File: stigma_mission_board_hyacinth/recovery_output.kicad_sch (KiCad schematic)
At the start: 19 parts, among them Q6 DMN2056U, Q7 AOSP21321, Q8 DMN2056U, Q9 AOSP21321, U9 INA181

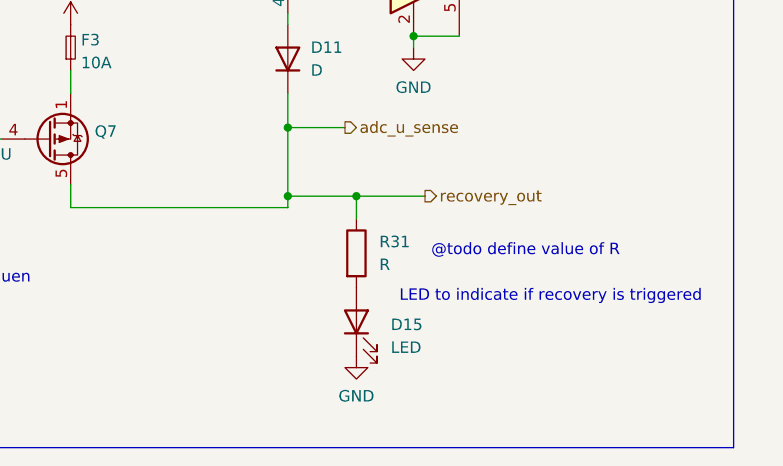
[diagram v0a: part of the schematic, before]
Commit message: rename recovery_output file
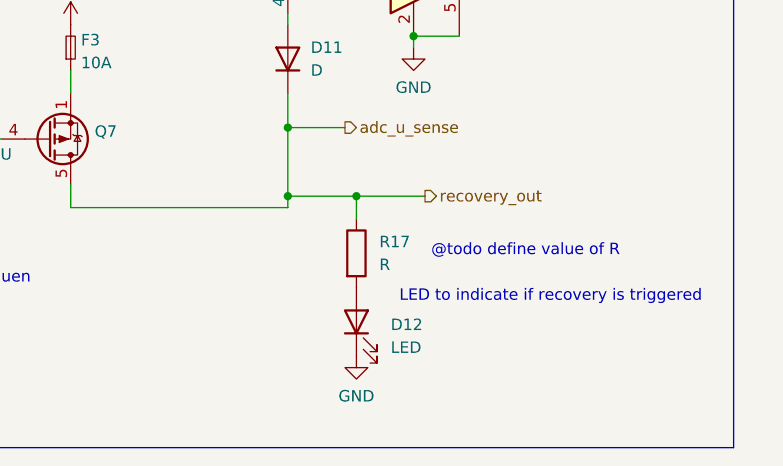
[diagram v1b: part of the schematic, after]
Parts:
- renumbered D15 to D12, R31 to R17

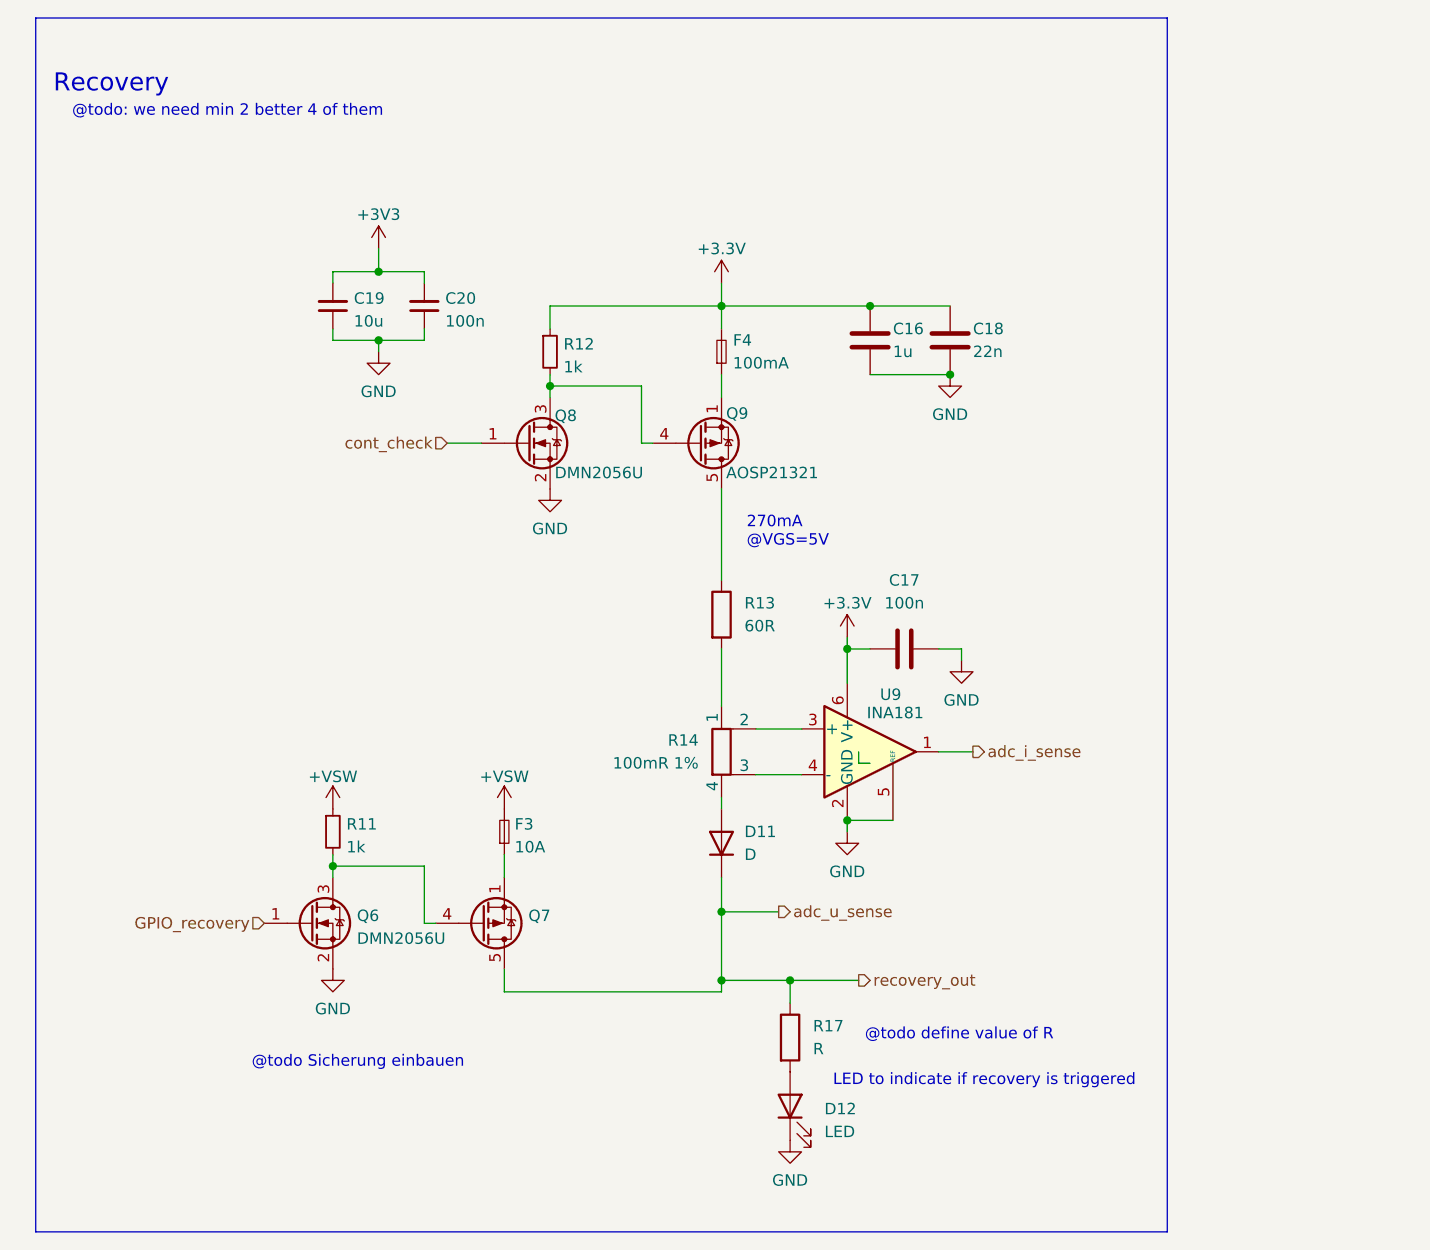
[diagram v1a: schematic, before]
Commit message: fix ethernet, add VH bus, fix voltage sensing
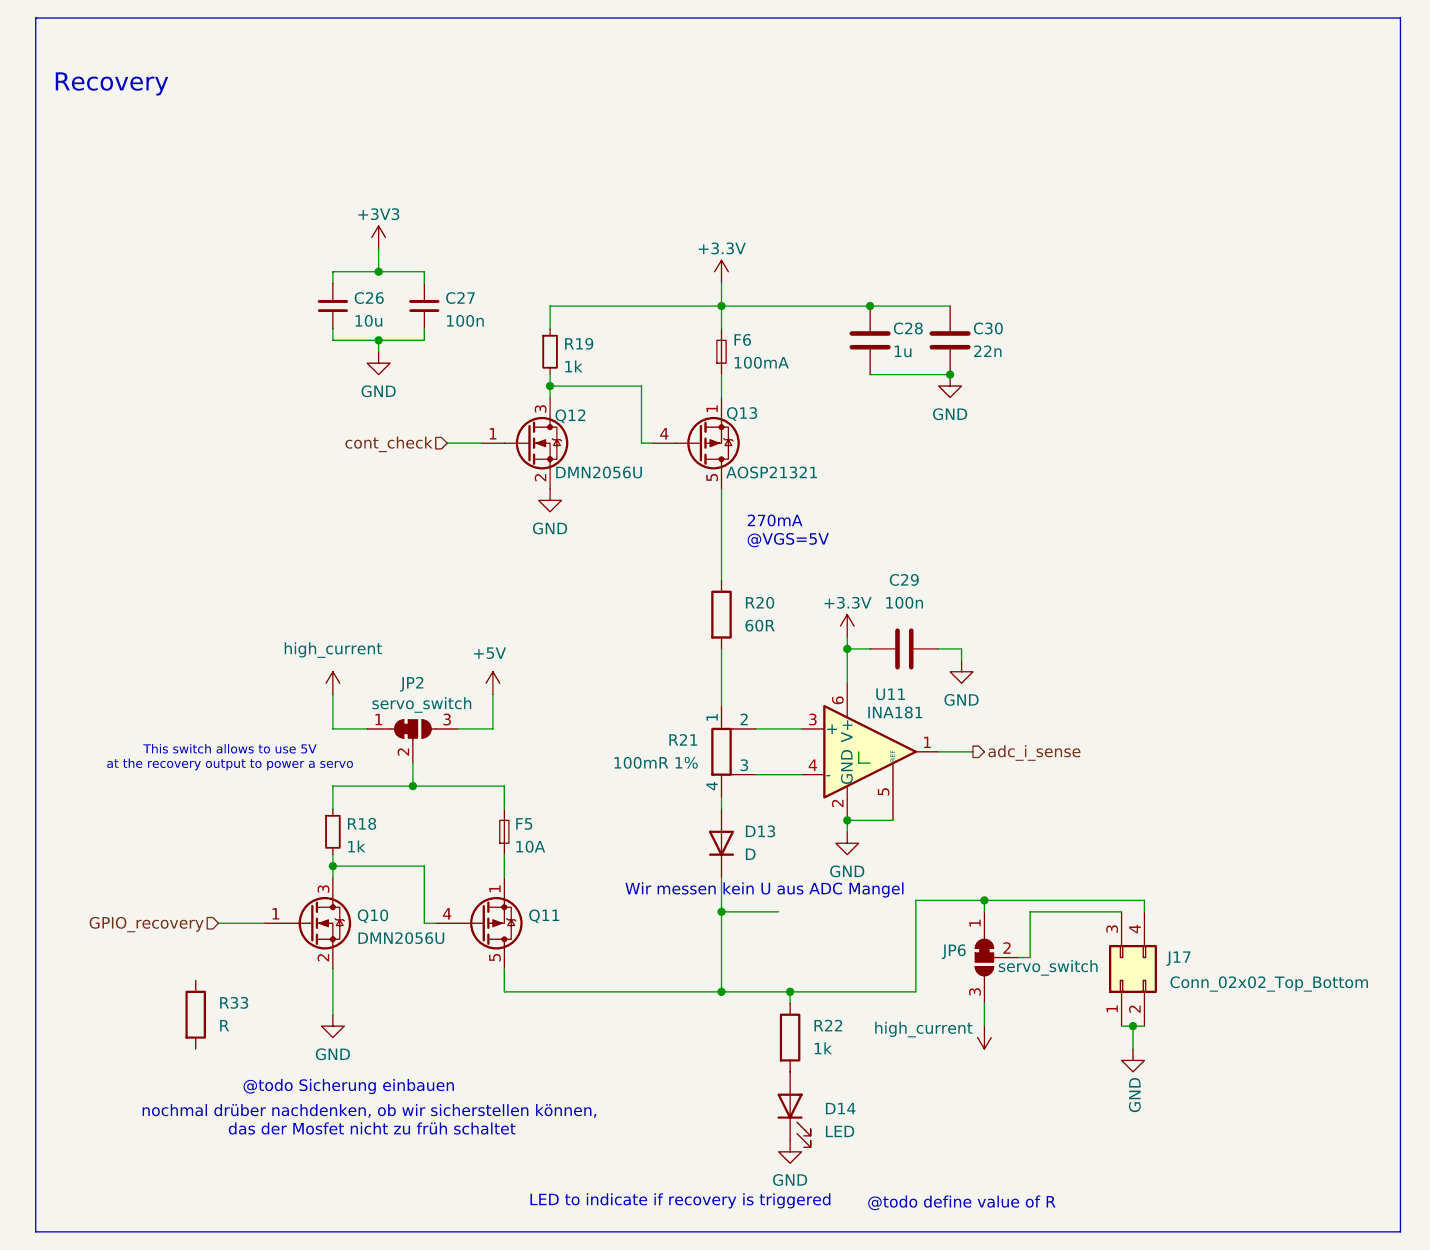
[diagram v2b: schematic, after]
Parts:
- added J17: Conn_02x02_Top_Bottom, symbol Connector_Generic:Conn_02x02_Top_Bottom
- added JP2, JP6: servo_switch, Jumper:SolderJumper-3_P1.3mm_Open_RoundedPad1.0x1.5mm, symbol Jumper:SolderJumper_3_Bridged12
- added R33: R, symbol Device:R
- R22: renamed from R17; value R -> 1k
- renumbered C19 to C26, C20 to C27, C16 to C28, C17 to C29, C18 to C30, D11 to D13, D12 to D14, F3 to F5, F4 to F6, Q6 to Q10, Q7 to Q11, Q8 to Q12, Q9 to Q13, R11 to R18, R12 to R19, R13 to R20, R14 to R21, U9 to U11
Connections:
- net GND: now also J17.1 (Pin_1), J17.2 (Pin_2)
- net +VSW: no longer names the net of F5.2, R18.1
- net +VSW: now also JP2.2 (C)
- net adc_u_sense: no longer names the net of D13.1 (K), Q11.5 (D), Q11.6 (D), Q11.7 (D), Q11.8 (D), R22.1
- net adc_u_sense: now also J17.4 (Pin_4), JP6.1 (A)
- new net: J17.3 (Pin_3), JP6.2 (C)
- new net +5V: JP2.3 (B)
- new net high_current: JP2.1 (A), JP6.3 (B)
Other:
- note added: "This switch allows to use 5V at the recovery output to power a servo"
- note added: "Wir messen kein U aus ADC Mangel"
- note added: "nochmal drüber nachdenken, ob wir sicherstellen können, das der Mosfet nicht zu früh schaltet"
- note removed: "@todo: we need min 2 better 4 of them"

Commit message: fixed a few small issues, added some part numbers and footprints
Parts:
- added C66: 10u, Capacitor_SMD:C_1206_3216Metric, symbol Device:C
- D13: value D -> NRVB130T1G; footprint (none) -> Diode_SMD:D_SOD-123; LCSC# (none) -> C917121
- R33: value R -> 10k
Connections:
- net GND: now also R33.2, C66.2
- net GPIO_recovery: now also R33.1
- net high_current: no longer JP6.3 (B)
- net adc_u_sense: now reaches D13.2 (A), R21.4
- net at F5.1, Q11.1 (S), Q11.2 (S)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: now also C66.1
- new net pwm_sig: JP6.3 (B)
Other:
- note added: "D"
- note added: "G"
- note added: "S"
- note added: "nochmal drüber nachdenken, ob wir sicherstellen können, das der Mosfet nicht zu früh schaltet -> ist kondensator ausreichend? -> verzögerung der spannung an DS"
- note removed: "@todo Sicherung einbauen"
- note removed: "Wir messen kein U aus ADC Mangel"
- note removed: "nochmal drüber nachdenken, ob wir sicherstellen können, das der Mosfet nicht zu früh schaltet"
- moved on the sheet: D13, J17, JP6, R33

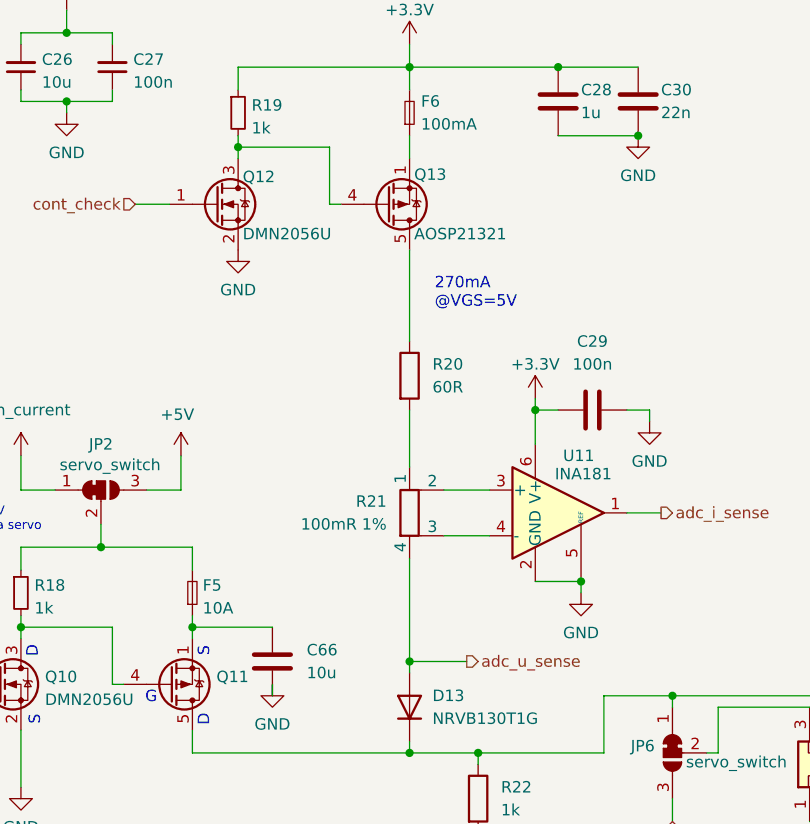
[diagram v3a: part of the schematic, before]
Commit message: changed mosfet to more suitable one
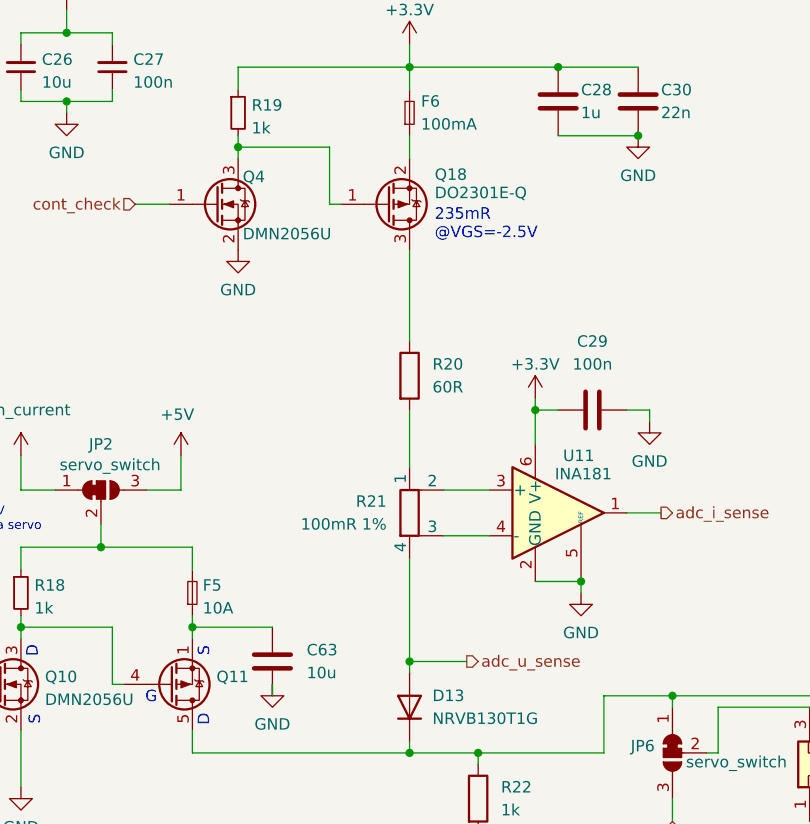
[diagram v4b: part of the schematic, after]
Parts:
- removed Q12: DMN2056U, Package_TO_SOT_SMD:SOT-23, symbol Transistor_FET:DMG2302U
- removed Q13: AOSP21321, Package_SO:SO-8_3.9x4.9mm_P1.27mm, symbol euroc_fc:AOSP21321
- added Q18: DO2301E-Q, Package_TO_SOT_SMD:SOT-23, symbol euroc_fc:AOSP21321
- added Q4: DMN2056U, Package_TO_SOT_SMD:SOT-23, symbol Transistor_FET:DMG2302U
- renumbered C66 to C63
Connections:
- net GND: now also Q4.2 (S)
- net cont_check: now also Q4.1 (G)
- net at R19.2: now also Q18.1 (G), Q4.3 (D)
- net at F6.1: now also Q18.2 (S)
- net at R20.1: now also Q18.3 (D)
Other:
- note added: "235mR @VGS=-2.5V"
- note removed: "270mA @VGS=5V"

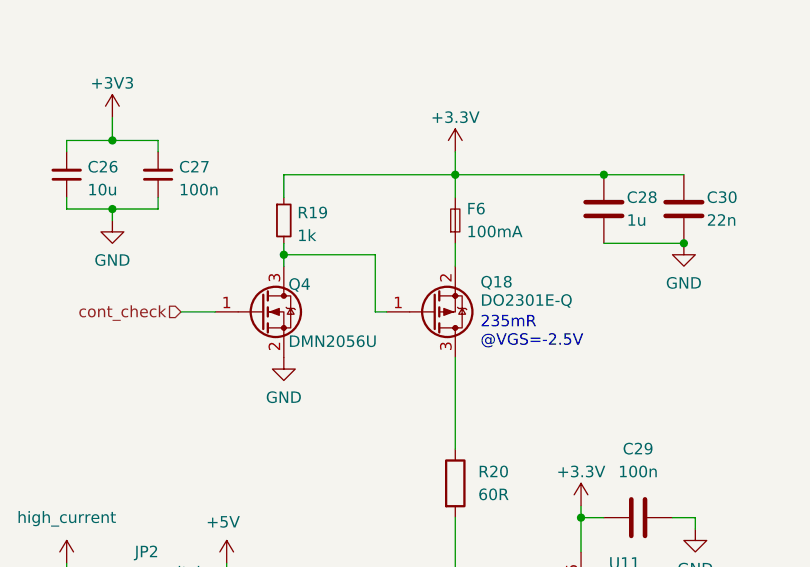
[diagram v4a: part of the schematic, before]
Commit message: changed vehicle bus connector numbering
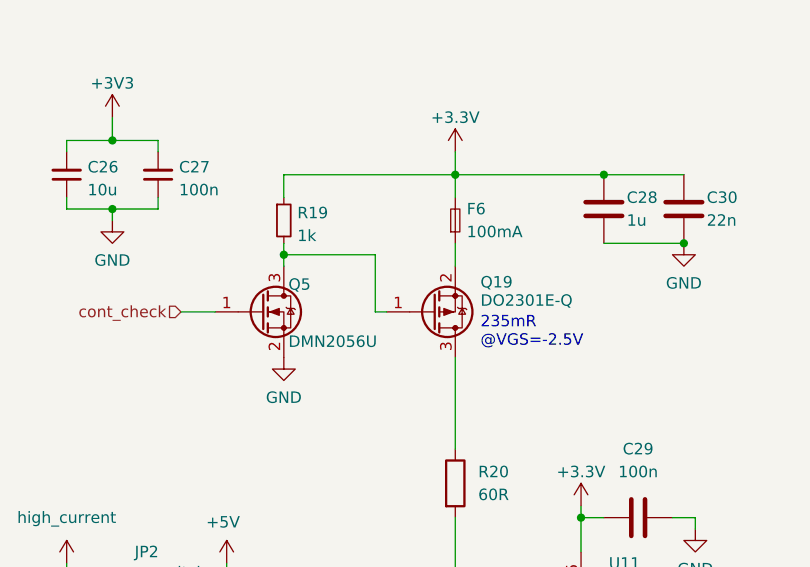
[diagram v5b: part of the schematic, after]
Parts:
- renumbered Q18 to Q19, Q4 to Q5
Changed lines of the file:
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@@
 		(on_board yes)
 		(dnp no)
-		(property "Reference" "Q18"
+		(property "Reference" "Q19"
 			(at 98.044 61.468 0)
 			(effects
@@
 		(on_board yes)
 		(dnp no)
-		(property "Reference" "Q4"
+		(property "Reference" "Q5"
 			(at 76.708 61.722 0)
 			(effects

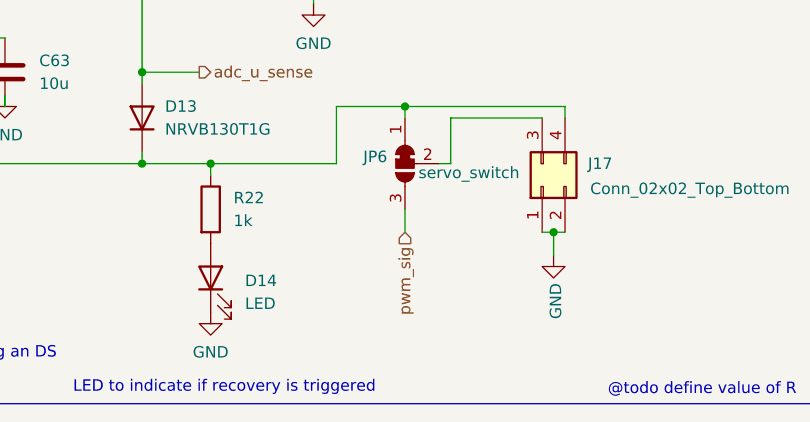
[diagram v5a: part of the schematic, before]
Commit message: add high_voltage to pwm signal again
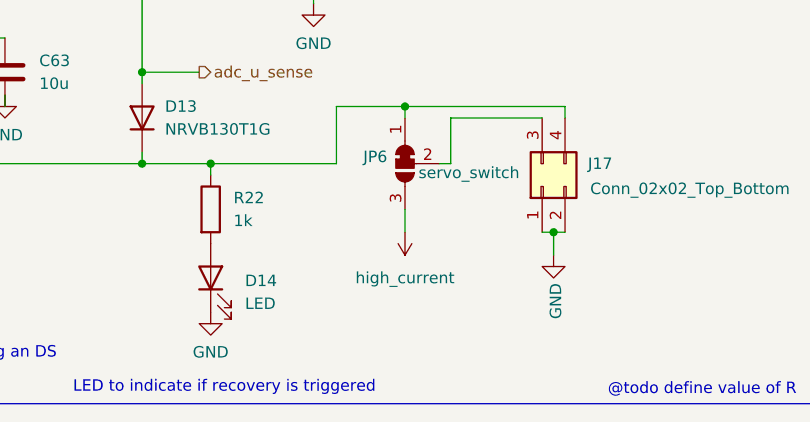
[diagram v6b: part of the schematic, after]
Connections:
- net pwm_sig is gone; now on net high_current: JP6.3 (B)
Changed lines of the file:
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@@
 		(shape input)
 		(at 64.77 64.77 180)
-		(fields_autoplaced yes)
 		(effects
 			(font
@@
 		(shape output)
 		(at 123.19 99.06 0)
-		(fields_autoplaced yes)
 		(effects
 			(font
@@
 		(shape input)
 		(at 39.37 118.11 180)
-		(fields_autoplaced yes)
 		(effects
 			(font
@@
 		)
 	)
-	(hierarchical_label "pwm_sig"
-		(shape input)
-		(at 124.46 133.35 270)
-		(fields_autoplaced yes)
-		(effects
-			(font
-				(size 1.27 1.27)
-			)
-			(justify right)
-		)
-	)
 	(hierarchical_label "adc_u_sense"
 		(shape output)
 		(at 101.6 115.57 0)
-		(fields_autoplaced yes)
 		(effects
 			(font
@@
 					(unit 1)
 				)
+			)
+		)
+	)
+	(symbol
+		(lib_id "power:+VSW")
+		(at 124.46 133.35 180)
+		(unit 1)
+		(exclude_from_sim no)
+		(in_bom yes)
+		(on_board yes)
+		(dnp no)
+		(fields_autoplaced yes)
+		(property "Reference" "#PWR0171"
+			(at 124.46 129.54 0)
+			(effects
+				(font
+					(size 1.27 1.27)
+				)
+				(hide yes)
+			)
+		)
+		(property "Value" "high_current"
+			(at 124.46 138.43 0)
+			(effects
+				(font
+					(size 1.27 1.27)
+				)
+			)
+		)
+		(property "Footprint" ""
+			(at 124.46 133.35 0)
+			(effects
+				(font
+					(size 1.27 1.27)
+				)
+				(hide yes)
+			)
+		)
+		(property "Datasheet" ""
+			(at 124.46 133.35 0)
+			(effects
+				(font
+					(size 1.27 1.27)
+				)
+				(hide yes)
+			)
+		)
+		(property "Description" ""
+			(at 124.46 133.35 0)
+			(effects
+				(font
+					(size 1.27 1.27)
+				)
+				(hide yes)
+			)
+		)
+		(pin "1"
+		)
+		(instances
+			(project "stigma_mission_board_hysteresis"
+				(path "/34e067c7-b84e-477a-88f3-7322f422dd23/1b0ab639-d420-4016-938c-453dcf1ed81d"
+					(reference "#PWR0172")
+					(unit 1)
+				)
+				(path "/34e067c7-b84e-477a-88f3-7322f422dd23/1e21a0b4-3701-4fea-ae6f-c1650f6b51b3"
+					(reference "#PWR0171")
+					(unit 1)
+				)
+				(path "/34e067c7-b84e-477a-88f3-7322f422dd23/4924f453-debe-420b-955f-34707f20b488"
+					(reference "#PWR0174")
+					(unit 1)
+				)
+				(path "/34e067c7-b84e-477a-88f3-7322f422dd23/9351aa18-d08f-4bdd-8577-c307d483b4c3"
+					(reference "#PWR0173")
+					(unit 1)
+				)
